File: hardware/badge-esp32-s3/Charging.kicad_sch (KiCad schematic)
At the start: 12 parts, among them P1 PH-2A_C2319, Q3 HL2301A, SW3 SK-12F04-G050, U4 TP4056, U5 FH2.54-09-02PZD

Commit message: schematic_pwr
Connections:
- net GND: now also P1.1; no longer P1.2
- net VBATT: now also P1.2; no longer P1.1
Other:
- moved on the sheet: C13
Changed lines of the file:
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@@
+	)
+	(junction
+		(at 177.8 90.17)
+		(diameter 0)
+		(color 0 0 0 0)
 	)
 	(junction
@@
 	)
 	(junction
+		(at 185.42 85.09)
+		(diameter 0)
+		(color 0 0 0 0)
+	)
+	(junction
 		(at 120.65 67.31)
 		(diameter 0)
@@
 	)
 	(junction
-		(at 185.42 90.17)
-		(diameter 0)
-		(color 0 0 0 0)
-	)
-	(junction
 		(at 106.68 73.66)
 		(diameter 0)
@@
 	(wire
 		(pts
-			(xy 185.42 76.2) (xy 185.42 90.17)
-		)
-		(stroke
-			(width 0)
-			(type default)
-		)
-	)
-	(wire
-		(pts
 			(xy 118.11 73.66) (xy 120.65 73.66)
 		)
@@
 	(wire
 		(pts
-			(xy 185.42 90.17) (xy 201.93 90.17)
-		)
-		(stroke
-			(width 0)
-			(type default)
-		)
-	)
-	(wire
-		(pts
 			(xy 185.42 106.68) (xy 177.8 106.68)
 		)
@@
 	(wire
 		(pts
+			(xy 177.8 95.25) (xy 177.8 90.17)
+		)
+		(stroke
+			(width 0)
+			(type default)
+		)
+	)
+	(wire
+		(pts
 			(xy 130.81 90.17) (xy 133.35 90.17)
 		)
@@
 	(wire
 		(pts
-			(xy 177.8 85.09) (xy 201.93 85.09)
-		)
-		(stroke
-			(width 0)
-			(type default)
-		)
-	)
-	(wire
-		(pts
 			(xy 88.9 58.42) (xy 88.9 63.5)
 		)
@@
 	(wire
 		(pts
+			(xy 177.8 90.17) (xy 201.93 90.17)
+		)
+		(stroke
+			(width 0)
+			(type default)
+		)
+	)
+	(wire
+		(pts
+			(xy 185.42 85.09) (xy 201.93 85.09)
+		)
+		(stroke
+			(width 0)
+			(type default)
+		)
+	)
+	(wire
+		(pts
 			(xy 106.68 91.44) (xy 106.68 101.6)
 		)
@@
 	(wire
 		(pts
+			(xy 177.8 90.17) (xy 177.8 85.09)
+		)
+		(stroke
+			(width 0)
+			(type default)
+		)
+	)
+	(wire
+		(pts
 			(xy 116.84 100.33) (xy 116.84 101.6)
 		)
@@
 	(wire
 		(pts
-			(xy 185.42 90.17) (xy 185.42 106.68)
-		)
-		(stroke
-			(width 0)
-			(type default)
-		)
-	)
-	(wire
-		(pts
-			(xy 177.8 92.71) (xy 177.8 106.68)
+			(xy 185.42 76.2) (xy 185.42 85.09)
+		)
+		(stroke
+			(width 0)
+			(type default)
+		)
+	)
+	(wire
+		(pts
+			(xy 177.8 102.87) (xy 177.8 106.68)
 		)
 		(stroke
@@
 		(pts
 			(xy 110.49 73.66) (xy 106.68 73.66)
+		)
+		(stroke
+			(width 0)
+			(type default)
+		)
+	)
+	(wire
+		(pts
+			(xy 185.42 85.09) (xy 185.42 106.68)
 		)
 		(stroke
@@
 	(symbol
 		(lib_id "PCM_JLCPCB-Capacitors:0603,10uF,(2)")
-		(at 177.8 88.9 0)
+		(at 177.8 99.06 0)
 		(unit 1)
 		(exclude_from_sim no)
@@
 		(fields_autoplaced yes)
 		(property "Reference" "C13"
-			(at 180.34 86.3599 0)
+			(at 180.34 96.5199 0)
 			(effects
 				(font
@@
 		)
 		(property "Value" "10uF"
-			(at 180.34 88.9 0)
+			(at 180.34 99.06 0)
 			(effects
 				(font
@@
 		)
 		(property "Footprint" "PCM_JLCPCB:C_0603"
-			(at 176.022 88.9 90)
+			(at 176.022 99.06 90)
 			(effects
 				(font
@@
 		)
 		(property "Datasheet" "https://www.lcsc.com/datasheet/lcsc_datasheet_2304140030_Samsung-Electro-Mechanics-CL10A106MA8NRNC_C96446.pdf"
-			(at 177.8 88.9 0)
+			(at 177.8 99.06 0)
 			(effects
 				(font
@@
 		)
 		(property "Description" "25V 10uF X5R ±20% 0603 Multilayer Ceramic Capacitors MLCC - SMD/SMT ROHS"
-			(at 177.8 88.9 0)
+			(at 177.8 99.06 0)
 			(effects
 				(font
@@
 		)
 		(property "LCSC" "C96446"
-			(at 177.8 88.9 0)
+			(at 177.8 99.06 0)
 			(effects
 				(font
@@
 		)
 		(property "Stock" "2627344"
-			(at 177.8 88.9 0)
+			(at 177.8 99.06 0)
 			(effects
 				(font
@@
 		)
 		(property "Price" "0.021USD"
-			(at 177.8 88.9 0)
+			(at 177.8 99.06 0)
 			(effects
 				(font
@@
 		)
 		(property "Process" "SMT"
-			(at 177.8 88.9 0)
+			(at 177.8 99.06 0)
 			(effects
 				(font
@@
 		)
 		(property "Minimum Qty" "20"
-			(at 177.8 88.9 0)
+			(at 177.8 99.06 0)
 			(effects
 				(font
@@
 		)
 		(property "Attrition Qty" "8"
-			(at 177.8 88.9 0)
+			(at 177.8 99.06 0)
 			(effects
 				(font
@@
 		)
 		(property "Class" "Basic Component"
-			(at 177.8 88.9 0)
+			(at 177.8 99.06 0)
 			(effects
 				(font
@@
 		)
 		(property "Category" "Capacitors,Multilayer Ceramic Capacitors MLCC - SMD/SMT"
-			(at 177.8 88.9 0)
+			(at 177.8 99.06 0)
 			(effects
 				(font
@@
 		)
 		(property "Manufacturer" "Samsung Electro-Mechanics"
-			(at 177.8 88.9 0)
+			(at 177.8 99.06 0)
 			(effects
 				(font
@@
 		)
 		(property "Part" "CL10A106MA8NRNC"
-			(at 177.8 88.9 0)
+			(at 177.8 99.06 0)
 			(effects
 				(font
@@
 		)
 		(property "Voltage Rated" "25V"
-			(at 180.34 91.44 0)
+			(at 180.34 101.6 0)
 			(effects
 				(font
@@
 		)
 		(property "Tolerance" "±20%"
-			(at 177.8 88.9 0)
+			(at 177.8 99.06 0)
 			(effects
 				(font
@@
 		)
 		(property "Capacitance" "10uF"
-			(at 177.8 88.9 0)
+			(at 177.8 99.06 0)
 			(effects
 				(font
@@
 		)
 		(property "Temperature Coefficient" "X5R"
-			(at 177.8 88.9 0)
-			(effects
-				(font
+			(at 177.8 99.06 0)
+			(effects
+				(font

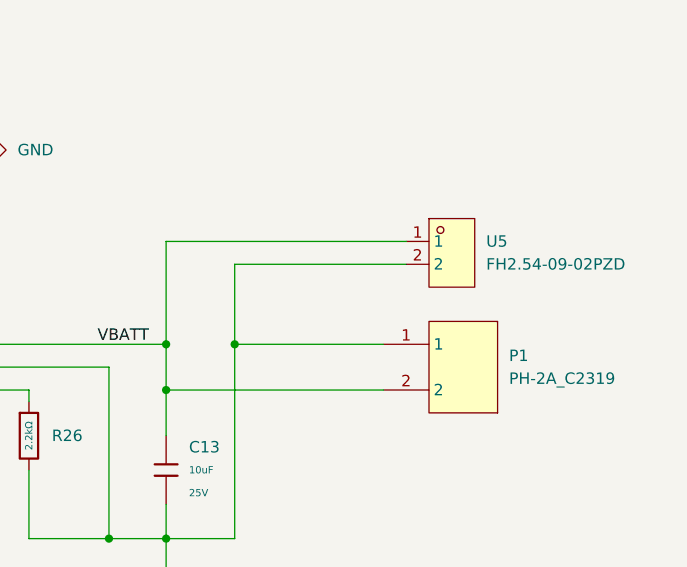
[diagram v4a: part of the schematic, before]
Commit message: delete_testing_pwr
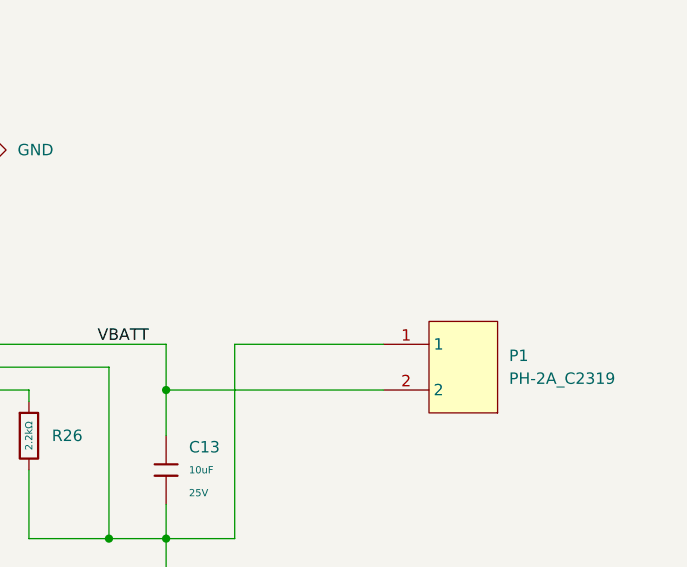
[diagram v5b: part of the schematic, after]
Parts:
- removed U5: FH2.54-09-02PZD, lcsc-lib:HDR-TH_2P-P2.54-V-M-5, symbol lcsc-lib:FH2.54-09-02PZD
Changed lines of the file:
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@@
-	)
-	(junction
-		(at 177.8 85.09)
-		(diameter 0)
-		(color 0 0 0 0)
 	)
 	(junction
@@
 	)
 	(junction
-		(at 185.42 85.09)
-		(diameter 0)
-		(color 0 0 0 0)
-	)
-	(junction
 		(at 120.65 67.31)
 		(diameter 0)
@@
 	(wire
 		(pts
-			(xy 204.47 73.66) (xy 177.8 73.66)
-		)
-		(stroke
-			(width 0)
-			(type default)
-		)
-	)
-	(wire
-		(pts
 			(xy 185.42 106.68) (xy 177.8 106.68)
 		)
@@
 	(wire
 		(pts
-			(xy 204.47 76.2) (xy 185.42 76.2)
-		)
-		(stroke
-			(width 0)
-			(type default)
-		)
-	)
-	(wire
-		(pts
 			(xy 162.56 106.68) (xy 171.45 106.68)
 		)
@@
 	(wire
 		(pts
-			(xy 177.8 73.66) (xy 177.8 85.09)
-		)
-		(stroke
-			(width 0)
-			(type default)
-		)
-	)
-	(wire
-		(pts
 			(xy 127 85.09) (xy 127 82.55)
 		)
@@
 		(pts
 			(xy 120.65 50.8) (xy 120.65 53.34)
-		)
-		(stroke
-			(width 0)
-			(type default)
-		)
-	)
-	(wire
-		(pts
-			(xy 185.42 76.2) (xy 185.42 85.09)
 		)
 		(stroke
@@
 					(unit 1)
 				)
-			)
-		)
-	)
-	(symbol
-		(lib_id "lcsc-lib:FH2.54-09-02PZD")
-		(at 209.55 74.93 0)
-		(unit 1)
-		(exclude_from_sim no)
-		(in_bom yes)
-		(on_board yes)
-		(dnp no)
-		(fields_autoplaced yes)
-		(property "Reference" "U5"
-			(at 213.36 73.6599 0)
-			(effects
-				(font
-					(size 1.27 1.27)
-				)
-				(justify left)
-			)
-		)
-		(property "Value" "FH2.54-09-02PZD"
-			(at 213.36 76.1999 0)
-			(effects
-				(font
-					(size 1.27 1.27)
-				)
-				(justify left)
-			)
-		)
-		(property "Footprint" "lcsc-lib:HDR-TH_2P-P2.54-V-M-5"
-			(at 209.55 83.82 0)
-			(effects
-				(font
-					(size 1.27 1.27)
-				)
-				(hide yes)
-			)
-		)
-		(property "Datasheet" ""
-			(at 209.55 74.93 0)
-			(effects
-				(font
-					(size 1.27 1.27)
-				)
-				(hide yes)
-			)
-		)
-		(property "Description" ""
-			(at 209.55 74.93 0)
-			(effects
-				(font
-					(size 1.27 1.27)
-				)
-				(hide yes)
-			)
-		)
-		(property "LCSC Part" "C7500771"
-			(at 209.55 86.36 0)
-			(effects
-				(font
-					(size 1.27 1.27)
-				)
-				(hide yes)
-			)
-		)
-		(pin "2"
-		)
-		(pin "1"
-		)
-		(instances
-			(project ""
-				(path "/e2af9a6c-dbe9-4de2-9ba6-ea213a7300ec/9131a646-b9dc-4004-a7df-1b58b7ca0b9a"
-					(reference "U5")
-					(unit 1)
-				)

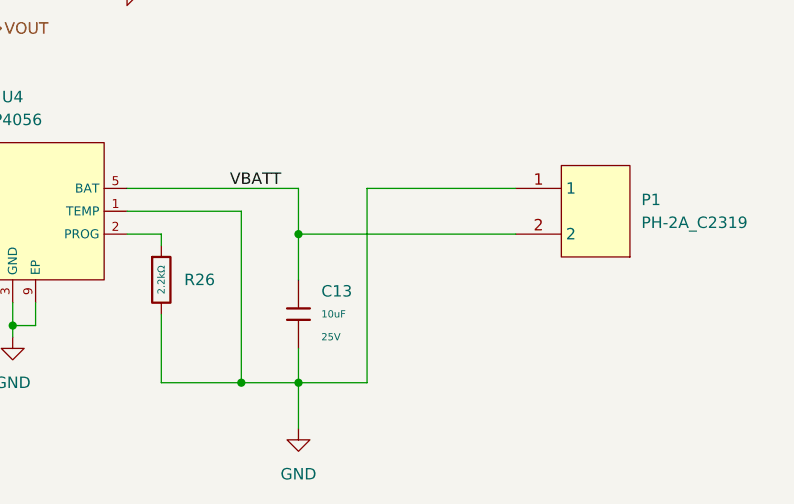
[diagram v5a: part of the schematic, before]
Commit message: reverse_battery_pins_back
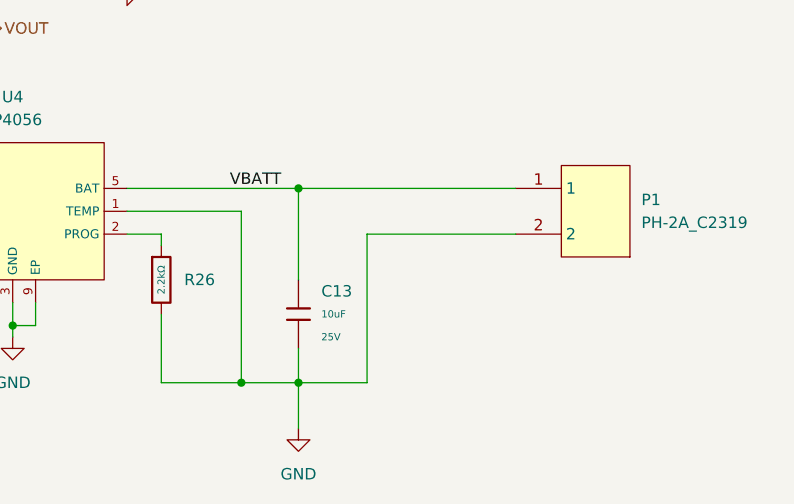
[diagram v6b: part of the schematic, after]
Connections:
- net GND: now also P1.2; no longer P1.1
- net VBATT: now also P1.1; no longer P1.2
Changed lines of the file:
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@@
 	)
 	(junction
-		(at 177.8 90.17)
+		(at 177.8 85.09)
 		(diameter 0)
 		(color 0 0 0 0)
@@
 	(wire
 		(pts
+			(xy 177.8 85.09) (xy 177.8 95.25)
+		)
+		(stroke
+			(width 0)
+			(type default)
+		)
+	)
+	(wire
+		(pts
 			(xy 146.05 100.33) (xy 146.05 97.79)
 		)
@@
 	(wire
 		(pts
-			(xy 177.8 95.25) (xy 177.8 90.17)
-		)
-		(stroke
-			(width 0)
-			(type default)
-		)
-	)
-	(wire
-		(pts
 			(xy 130.81 90.17) (xy 133.35 90.17)
 		)
@@
 	(wire
 		(pts
-			(xy 177.8 90.17) (xy 201.93 90.17)
-		)
-		(stroke
-			(width 0)
-			(type default)
-		)
-	)
-	(wire
-		(pts
-			(xy 185.42 85.09) (xy 201.93 85.09)
+			(xy 177.8 85.09) (xy 201.93 85.09)
+		)
+		(stroke
+			(width 0)
+			(type default)
+		)
+	)
+	(wire
+		(pts
+			(xy 185.42 90.17) (xy 201.93 90.17)
 		)
 		(stroke
@@
 	(wire
 		(pts
-			(xy 177.8 90.17) (xy 177.8 85.09)
-		)
-		(stroke
-			(width 0)
-			(type default)
-		)
-	)
-	(wire
-		(pts
 			(xy 116.84 100.33) (xy 116.84 101.6)
 		)
@@
 	(wire
 		(pts
-			(xy 185.42 85.09) (xy 185.42 106.68)
-		)
-		(stroke
+			(xy 185.42 90.17) (xy 185.42 106.68)
+		)
+		(stroke

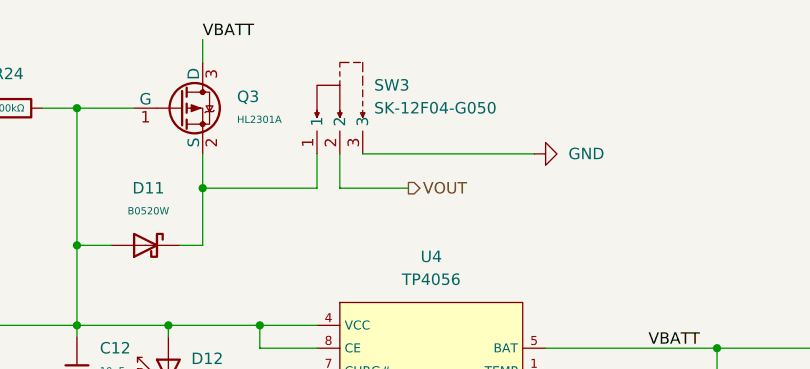
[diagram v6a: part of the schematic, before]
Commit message: Re-added the power switch label.
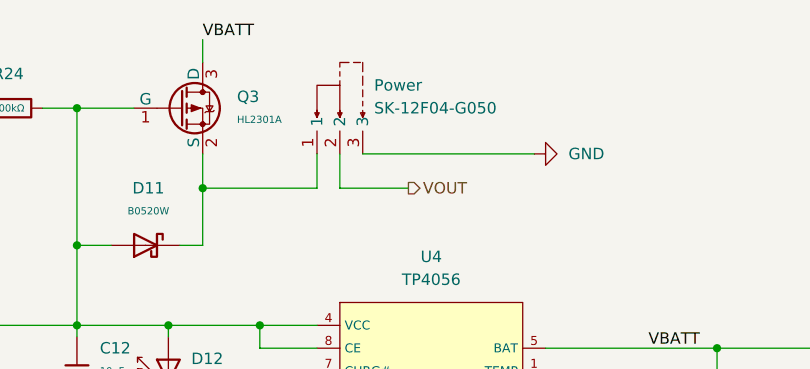
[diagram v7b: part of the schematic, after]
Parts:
- renumbered SW3 to Power
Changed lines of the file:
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@@
 		(dnp no)
 		(fields_autoplaced yes)
-		(property "Reference" "SW3"
+		(property "Reference" "Power"
 			(at 139.7 55.8799 0)
 			(effects
@@
 			(project "badge-esp32-s3"
 				(path "/e2af9a6c-dbe9-4de2-9ba6-ea213a7300ec/9131a646-b9dc-4004-a7df-1b58b7ca0b9a"
-					(reference "SW3")
+					(reference "Power")
 					(unit 1)
 				)

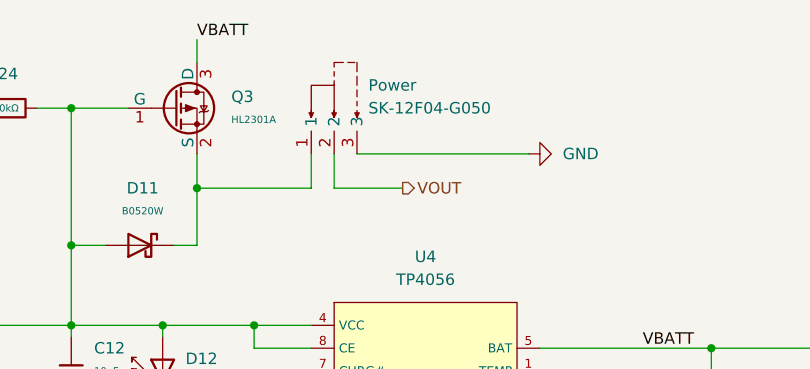
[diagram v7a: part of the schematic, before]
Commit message: Added thicker traces for the 5V circuit and added a TVS diode.
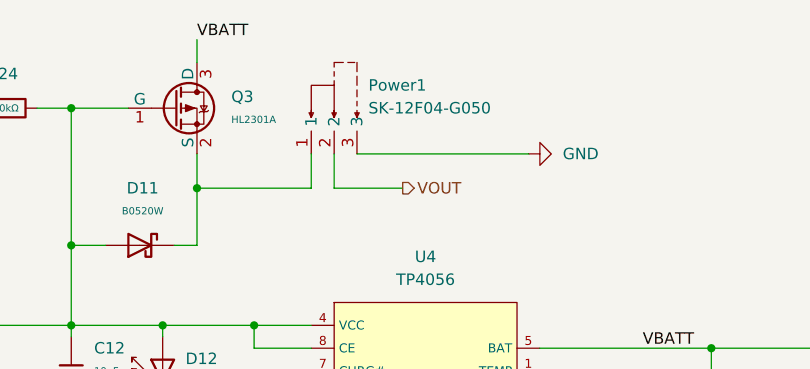
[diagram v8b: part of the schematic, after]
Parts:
- renumbered Power to Power1
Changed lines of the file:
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@@
 		(dnp no)
 		(fields_autoplaced yes)
-		(property "Reference" "Power"
+		(property "Reference" "Power1"
 			(at 139.7 55.8799 0)
 			(effects
@@
 			(project "badge-esp32-s3"
 				(path "/e2af9a6c-dbe9-4de2-9ba6-ea213a7300ec/9131a646-b9dc-4004-a7df-1b58b7ca0b9a"
-					(reference "Power")
+					(reference "Power1")
 					(unit 1)
 				)
